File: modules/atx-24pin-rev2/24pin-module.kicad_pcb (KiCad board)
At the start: 4 copper layers, 110 x 75.5 mm, 2 parts, among them J3 ATX-24 (PSU), J4 ATX-24 (MB)

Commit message: Spine complete.
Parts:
- added C1: 1uF, cec-Capacitor_SMD:C_0603_1608Metric, F.Cu at (241.5, 127.7)
- added C10: 100nF, cec-Capacitor_SMD:C_0402_1005Metric, F.Cu at (243.4, 88.0)
- added C11: 100nF, cec-Capacitor_SMD:C_0402_1005Metric, F.Cu at (243.4, 89.9)
- added C12: 100nF, cec-Capacitor_SMD:C_0402_1005Metric, F.Cu at (243.4, 91.9)
- added C13: 100nF, cec-Capacitor_SMD:C_0402_1005Metric, F.Cu at (243.4, 93.9)
- added C14: 100nF, cec-Capacitor_SMD:C_0402_1005Metric, F.Cu at (243.4, 95.8)
- added C15: 10µF, cec-Capacitor_SMD:C_0805_2012Metric, F.Cu at (241.8, 120.8)
- added C2: 1uF, cec-Capacitor_SMD:C_0603_1608Metric, F.Cu at (241.5, 130.2)
- added C3: 100nF, cec-Capacitor_SMD:C_0402_1005Metric, F.Cu at (240.5, 88.0)
- added C4: 100nF, cec-Capacitor_SMD:C_0402_1005Metric, F.Cu at (240.5, 89.9)
- added C5: 100nF, cec-Capacitor_SMD:C_0402_1005Metric, F.Cu at (240.5, 91.9)
- added C6: 100nF, cec-Capacitor_SMD:C_0402_1005Metric, F.Cu at (240.5, 93.9)
- added C7: 10µF, cec-Capacitor_SMD:C_0805_2012Metric, F.Cu at (241.8, 114.8)
- added C8: 1µF, cec-Capacitor_SMD:C_0805_2012Metric, F.Cu at (241.8, 117.8)
- added C9: 100nF, cec-Capacitor_SMD:C_0402_1005Metric, F.Cu at (240.5, 95.8)
- added D1: D_Schottky, cec-Diode_SMD:D_SMA, F.Cu at (225.4, 129.1)
- added D2: LED, cec-LED_SMD:LED_0603_1608Metric, F.Cu at (241.6, 123.6)
- added J1: TO-HUB, cec-Connector_RJ:RJ45_Amphenol_54602-x08_Horizontal, F.Cu at (116.2, 130.9)
- added J2: TO-HUB-PWR, cec-Connector_JST:JST_XH_S2B-XH-A_1x02_P2.50mm_Horizontal, F.Cu at (105.8, 135.6)
- added J5: USB_C_Receptacle_USB2.0_16P, cec-Connector_USB:USB_C_Receptacle_XKB_U262-16XN-4BVC11, F.Cu at (199.4, 59.8)
- added R1: R_ID (OQ-6), cec-Resistor_SMD:R_0402_1005Metric, F.Cu at (232.2, 127.4)
- added R10: 1kΩ, cec-Resistor_SMD:R_0402_1005Metric, F.Cu at (238.0, 131.4)
- added R2: 10kΩ, cec-Resistor_SMD:R_0402_1005Metric, F.Cu at (232.2, 129.4)
- added R3: 2.2kΩ, cec-Resistor_SMD:R_0402_1005Metric, F.Cu at (232.2, 131.4)
- added R4: 2.2kΩ, cec-Resistor_SMD:R_0402_1005Metric, F.Cu at (235.1, 127.4)
- added R5: 5.1kΩ, cec-Resistor_SMD:R_0402_1005Metric, F.Cu at (235.1, 129.4)
- added R6: 5.1kΩ, cec-Resistor_SMD:R_0402_1005Metric, F.Cu at (235.1, 131.4)
- added R7: 1kΩ, cec-Resistor_SMD:R_0402_1005Metric, F.Cu at (238.0, 127.4)
- added R9: 1kΩ, cec-Resistor_SMD:R_0402_1005Metric, F.Cu at (238.0, 129.4)
- added RS1: R002, cec-Resistor_SMD:R_2512_6332Metric, F.Cu at (124.5, 85.0)
- added RS2: R002, cec-Resistor_SMD:R_2512_6332Metric, F.Cu at (137.0, 92.5)
- added RS5: R002, cec-Resistor_SMD:R_2512_6332Metric, F.Cu at (150.5, 101.0)
- added RS6: R025, cec-Resistor_SMD:R_Shunt_Vishay_WSK2512_6332Metric_T1.19mm, F.Cu at (164.0, 109.5)
- added SW1: SW_Push, cec-Button_Switch_SMD:Panasonic_EVQPUJ_EVQPUA, F.Cu at (235.2, 117.1)
- added SW2: SW_Push, cec-Button_Switch_SMD:Panasonic_EVQPUJ_EVQPUA, F.Cu at (235.2, 123.6)
- added U1: ESP32-S3-MINI-1-N4R2, cec-RF_Module:ESP32-S2-MINI-1_NoAntKeepout, F.Cu at (210.7, 102.3)
- added U10: INA228, cec-Package_SO:VSSOP-10_3x3mm_P0.5mm, F.Cu at (124.5, 90.5)
- added U11: INA228, cec-Package_SO:VSSOP-10_3x3mm_P0.5mm, F.Cu at (137.0, 98.0)
- added U12: INA228, cec-Package_SO:VSSOP-10_3x3mm_P0.5mm, F.Cu at (150.5, 106.5)
- added U13: INA228, cec-Package_SO:VSSOP-10_3x3mm_P0.5mm, F.Cu at (163.5, 102.5)
- added U2: TJA1462A, cec-Package_SO:SOIC-8_3.9x4.9mm_P1.27mm, F.Cu at (238.2, 104.2)
- added U3: LP5907MFX-3.3, cec-Package_TO_SOT_SMD:SOT-23-5, F.Cu at (236.5, 89.4)
- added U4: 74LVC1G17, cec-Package_TO_SOT_SMD:SOT-23-5, F.Cu at (236.5, 94.0)
- added U5: 74LVC1G17, cec-Package_TO_SOT_SMD:SOT-23-5, F.Cu at (236.5, 98.6)
- moved J3 114.4 mm to (102.5, 125.4)
- moved J4 56.7 mm to (113.9, 69.8), turned to 0 degrees
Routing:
- net +5VSB: track 0.00 -> 128.1 mm, vias 0 -> 4
- net /RAIL5VSB_LO: track 0.00 -> 76.7 mm, vias 0 -> 4
- net /RAIL3V3_LO: track 0.00 -> 52.9 mm, vias 0 -> 25
- net /RAIL3V3_HI: track 0.00 -> 51.2 mm, vias 0 -> 25
- net /RAIL5V_LO: vias 0 -> 50
- net /RAIL5V_HI: vias 0 -> 25
- net /RAIL12V_LO: vias 0 -> 25
- net /RAIL12V_HI: vias 0 -> 25
- added copper zone on B.Cu, net /RAIL12V_HI
- added copper zone on F.Cu, net /RAIL12V_HI
- added copper zone on B.Cu, net /RAIL12V_LO
- added copper zone on F.Cu, net /RAIL12V_LO
- added copper zone on F.Cu, net /RAIL3V3_HI
- added copper zone on In2.Cu, net /RAIL3V3_HI
- added copper zone on F.Cu, net /RAIL3V3_LO
- added copper zone on In2.Cu, net /RAIL3V3_LO
- added copper zone on F.Cu, net /RAIL5V_HI
- added copper zone on In2.Cu, net /RAIL5V_HI
- added copper zone on B.Cu, net /RAIL5V_LO
- added copper zone on F.Cu, net /RAIL5V_LO
- added copper zone on In2.Cu, net /RAIL5V_LO
- added copper zone on In1.Cu, net GND
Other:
- board size 110 x 75.5 mm -> 82.9 x 79 mm

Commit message: All symbols placed, handoff to quilter.
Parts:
- moved C6 120.3 mm to (123.0, 119.5), turned to 180 degrees
- moved SW1 116.9 mm to (118.5, 110.0)
- moved C10 115.9 mm to (127.5, 89.5), turned to -90 degrees
- moved U2 111.5 mm to (128.0, 121.5), turned to 180 degrees
- moved C4 111.5 mm to (133.5, 121.0)
- moved SW2 108.5 mm to (127.5, 110.0)
- moved C8 107.2 mm to (136.5, 138.0)
- moved R10 104.7 mm to (135.0, 112.5), turned to 180 degrees
- moved C11 103.6 mm to (140.0, 97.0), turned to -90 degrees
- moved R1 102.2 mm to (130.0, 128.5)
- moved C9 101.0 mm to (140.5, 109.5), turned to -90 degrees
- moved C14 100.3 mm to (144.0, 109.5), turned to -90 degrees
- moved U5 99.4 mm to (138.1, 112.5)
- moved C3 96.9 mm to (157.0, 137.0), turned to -90 degrees
- moved D2 95.7 mm to (146.0, 119.5), turned to -90 degrees
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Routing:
- net +5VSB: track 128.1 -> 233.5 mm, vias 4 -> 6
- net Net-(J3--12V): track 0.00 -> 66.1 mm
- net GND: track 0.00 -> 61.7 mm, vias 0 -> 20
- net Net-(J3-PWR_OK): track 0.00 -> 60.2 mm
- net /GPIO0: track 0.00 -> 58.0 mm, vias 0 -> 2
- net +3V3: track 0.00 -> 55.6 mm, vias 0 -> 3
- net Net-(J3-PS_ON#): track 0.00 -> 45.2 mm
- net /EN: track 0.00 -> 39.3 mm
- net Net-(D1-A): track 0.00 -> 18.8 mm
- net /CAN1_P: track 0.00 -> 17.8 mm
- net /RAIL5V_LO: track 0.00 -> 10.1 mm
- net /RAIL3V3_LO: track 52.9 -> 62.9 mm
- net /RAIL12V_LO: track 0.00 -> 10.1 mm
- net /CAN1_N: track 0.00 -> 9.29 mm
- net Net-(RS6-S1): track 0.00 -> 7.96 mm
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
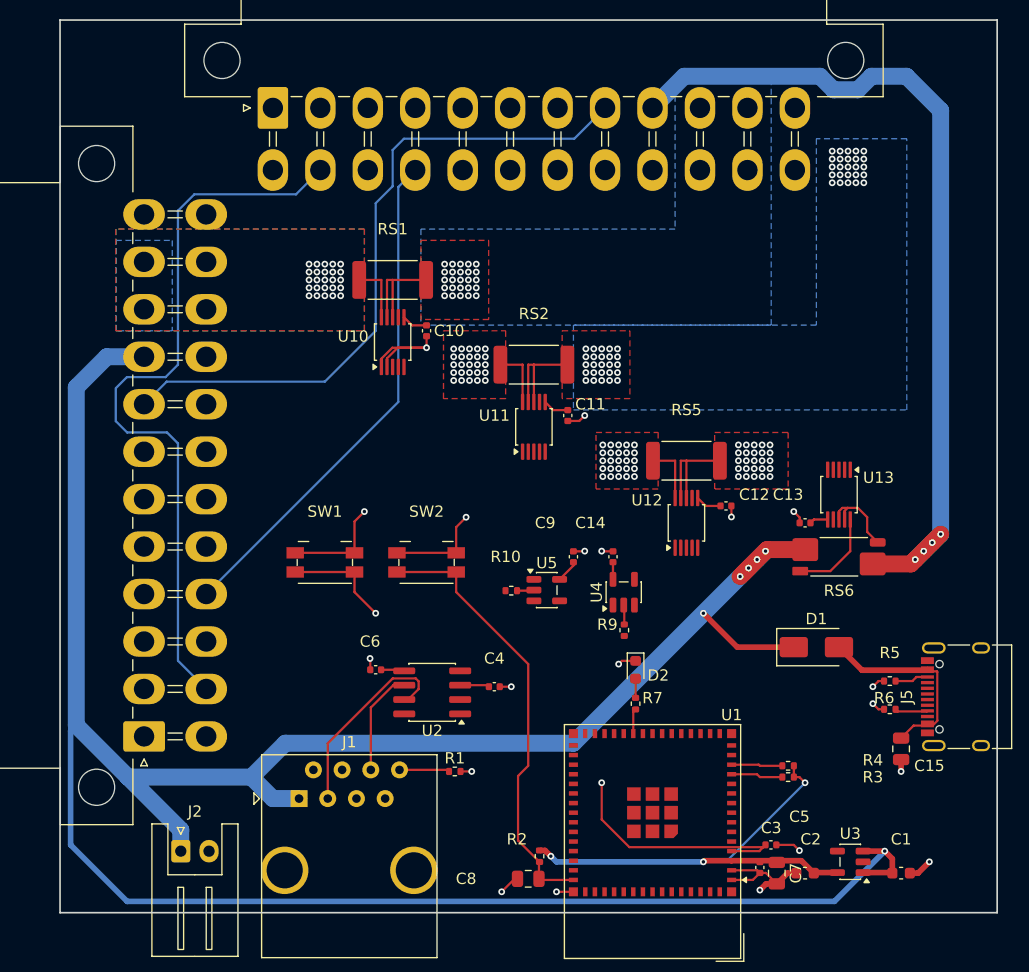
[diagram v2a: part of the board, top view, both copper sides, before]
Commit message: Finished routing for 24Pin Rev2 and added DRC. Fiducials added.
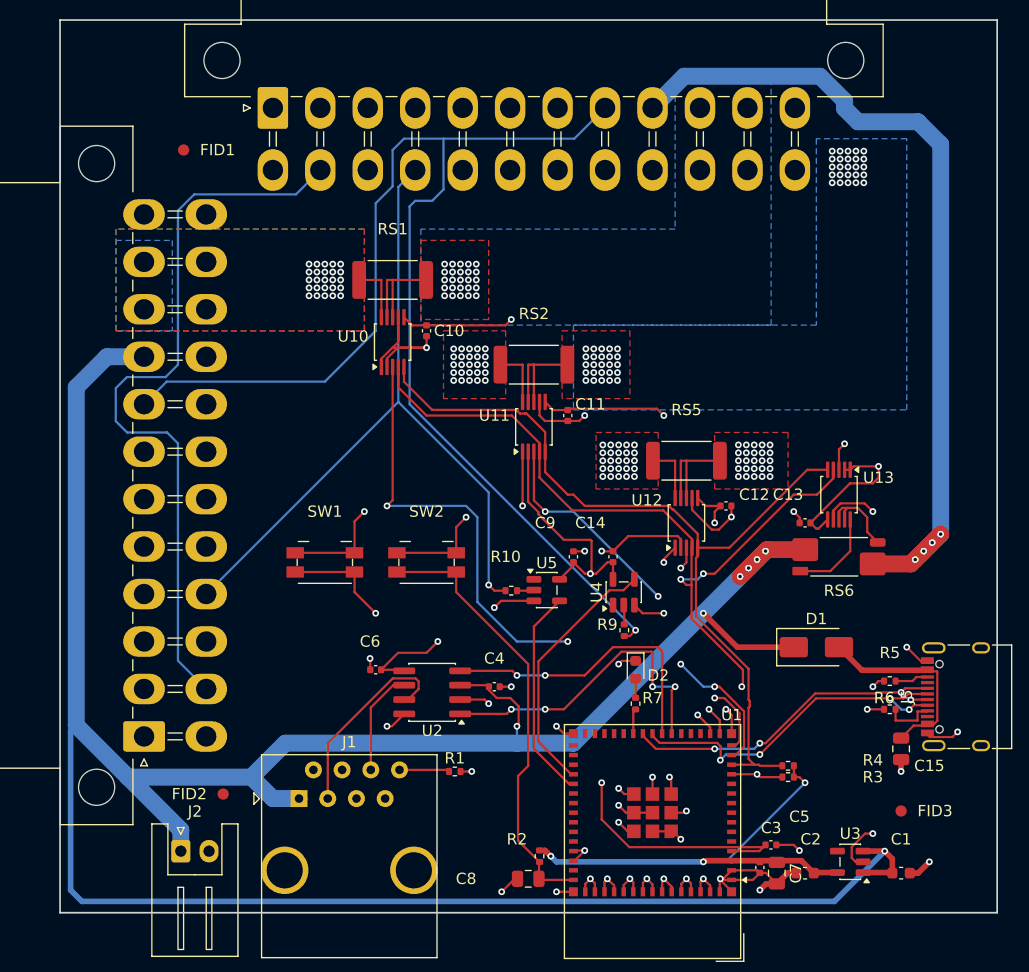
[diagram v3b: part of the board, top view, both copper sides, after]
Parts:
- added FID1: Fiducial_1mm_Mask2mm, cec-Fiducial:Fiducial_1mm_Mask2mm, F.Cu at (106.0, 73.5)
- added FID2: Fiducial_1mm_Mask2mm, cec-Fiducial:Fiducial_1mm_Mask2mm, F.Cu at (109.5, 130.5)
- added FID3: Fiducial_1mm_Mask2mm, cec-Fiducial:Fiducial_1mm_Mask2mm, F.Cu at (169.5, 132.0)
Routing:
- net +3V3: track 55.6 -> 218.8 mm, vias 3 -> 10
- net GND: track 61.7 -> 157.4 mm, vias 20 -> 47
- net Net-(U1-IO8): track 4.59 -> 82.2 mm, vias 0 -> 4
- net Net-(U1-IO9): track 4.53 -> 76.7 mm
- net Net-(U1-IO10): track 0.00 -> 60.6 mm, vias 0 -> 4
- net Net-(J3-PWR_OK): track 60.2 -> 115.3 mm, vias 0 -> 1
- net Net-(U1-IO11): track 0.00 -> 42.7 mm, vias 0 -> 3
- net Net-(U1-IO13): track 0.00 -> 40.2 mm, vias 0 -> 2
- net /USB_D-: track 0.00 -> 32.5 mm, vias 0 -> 4
- net /USB_D+: track 0.00 -> 30.7 mm, vias 0 -> 4
- net Net-(U1-IO17): track 0.00 -> 28.6 mm, vias 0 -> 4
- net Net-(U1-IO18): track 0.00 -> 26.5 mm, vias 0 -> 2
- net Net-(U1-IO38): track 0.00 -> 22.9 mm
- net Net-(J3-PS_ON#): track 45.2 -> 66.4 mm, vias 0 -> 1
- net Net-(U1-IO39): track 0.00 -> 18.8 mm
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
